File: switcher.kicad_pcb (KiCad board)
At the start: 2 copper layers, 137.5 x 100 mm, 67 parts, among them K1 RELAY, P1 CONN_01X02, P10 CONN_01X04, P11 CONN_01X04, P12 CONN_01X04, P13 CONN_01X04, P2 CONN_01X02, P3 CONN_01X04, P4 CONN_01X04, P5 CONN_01X04, P6 CONN_01X02, P7 CONN_01X04, P8 CONN_01X04, P9 BDM, Q1 BC237, SW1 RESET, SW2 SP3T, T1 TRANSFO, U1 MC9S08SH8, U10 4N25, U11 4N25, U12 4N25, U13 4N25, U14 4N25, U2 78L05, U3 4N25, U4 4N25, U5 4N25, U6 4N25, U7 4N25, U8 4N25, U9 4N25

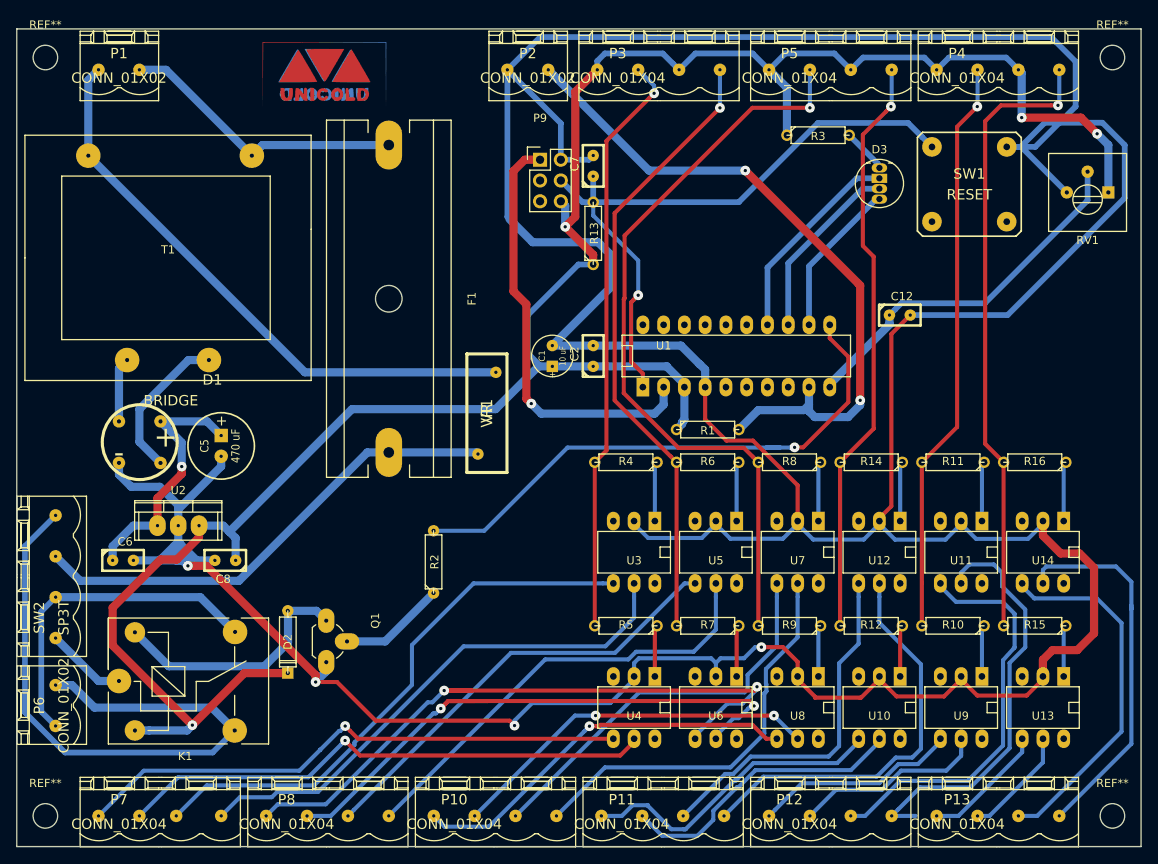
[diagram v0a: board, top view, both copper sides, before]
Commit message: cambio relay
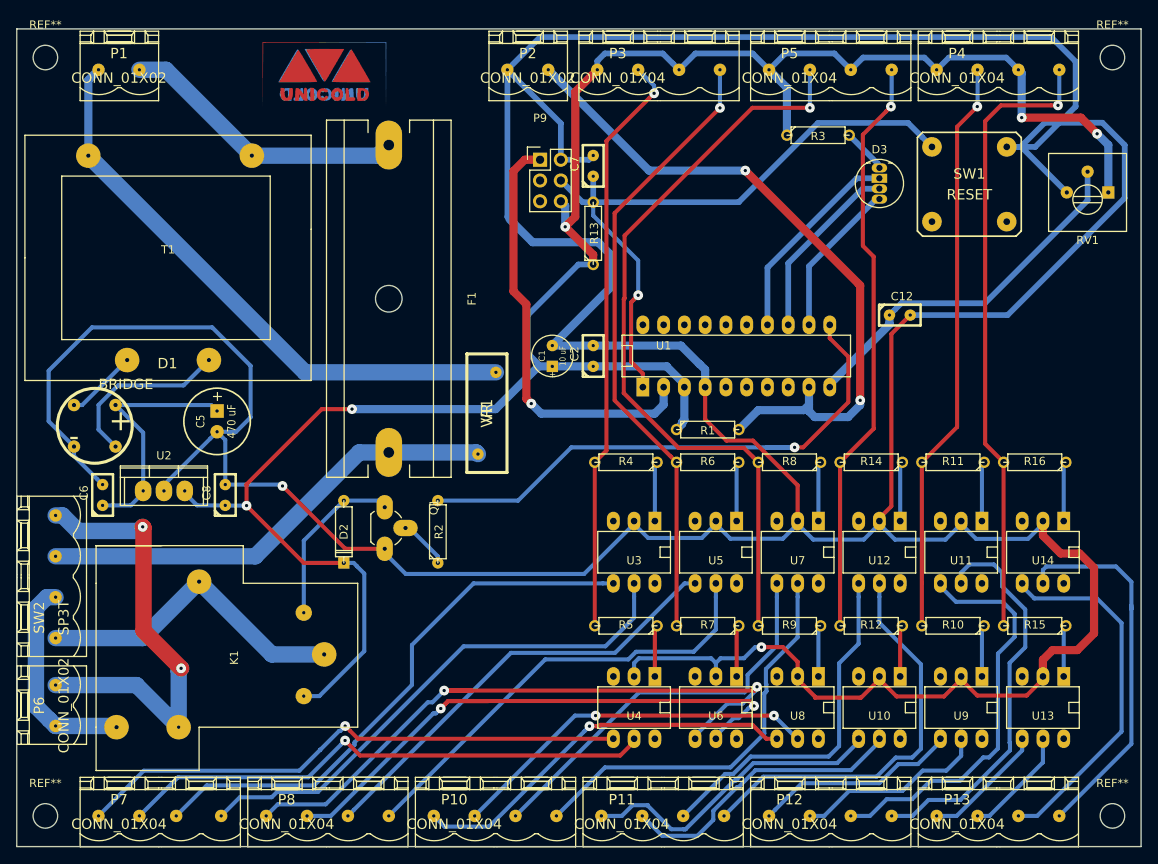
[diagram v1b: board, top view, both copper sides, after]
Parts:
- K1: footprint Relays_ThroughHole:Relay_SANYOU_SRD_Series_Form_C -> locales:RELAY-HJQ-15F
- moved Q1 15.6 mm to (119.5, 88.5)
- moved D2 15.1 mm to (114.5, 91.5)
- moved K1 13.5 mm to (100.2, 106.9), turned to 90 degrees
- moved C6 8.38 mm to (85.0, 87.0), turned to 90 degrees
- moved C8 8.00 mm to (100.0, 87.0), turned to 90 degrees
- moved D1 5.85 mm to (81.5, 76.0)
- moved U2 4.60 mm to (92.5, 86.5)
- moved R2 3.72 mm to (126.0, 91.5)
- moved C5 3.04 mm to (99.0, 78.0)
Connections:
- K1 pad 1: /C -> /NC
- K1 pad 2: /vreg -> /NA
- K1 pad 3: /NA -> /C
- K1 pad 4: /NC -> /vreg
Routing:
- net /C: track 9.92 -> 39.4 mm
- net /NA: track 78.6 -> 55.4 mm, vias 0 -> 2
- net /vreg: track 275.7 -> 255.9 mm, vias 4 -> 5
- net /NC: track 40.9 -> 25.9 mm
- net GND: track 557.2 -> 570.7 mm, vias 4 -> 2
- net Net-(D2-Pad1): track 30.7 -> 21.1 mm
- net Net-(Q1-Pad2): track 13.0 -> 6.20 mm
- net Net-(D1-Pad2): track 18.6 -> 21.7 mm
- net Net-(P12-Pad4): track 51.7 -> 49.0 mm
- net Net-(R2-Pad2): track 69.9 -> 71.3 mm
- net /24V: track 31.4 -> 30.5 mm, vias 1 -> 0
- net Net-(D1-Pad4): track 7.91 -> 8.78 mm
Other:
- net class Default: clearance 0.4 -> 0.35
- net class POTENCIA: trace_width 1 -> 2
- rule trace_clearance: 0.4 -> 0.35

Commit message: di vueltas el relay
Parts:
- K1: moved to B.Cu
- turned K1 to 270 degrees
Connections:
- K1 pad 4: /vreg -> Net-(D2-Pad1)
- K1 pad 5: Net-(D2-Pad1) -> /vreg
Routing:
- net /C: track 39.4 -> 54.7 mm
- net /NC: track 25.9 -> 33.8 mm
- net /vreg: track 255.9 -> 258.6 mm
- net Net-(D2-Pad1): track 21.1 -> 21.9 mm
- net /NA: track 55.4 -> 55.2 mm, vias 2 -> 3
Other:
- net class Default: trace_width 0.5 -> 2
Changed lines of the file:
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@@
     (links 125)
     (no_connects 0)
-    (area 74.449999 29.949999 212.050001 130.050001)
+    (area 71.361474 28.2245 217.140046 132.37626)
     (thickness 1.6)
     (drawings 4)
-    (tracks 668)
+    (tracks 681)
     (zones 0)
     (modules 67)
@@
   )
   (setup
-    (last_trace_width 0.5)
+    (last_trace_width 2)
     (trace_clearance 0.35)
     (zone_clearance 0.508)
@@
     (mod_text_size 1 1)
     (mod_text_width 0.15)
-    (pad_size 3 3)
-    (pad_drill 0.5)
+    (pad_size 2 2)
+    (pad_drill 0.4)
     (pad_to_mask_clearance 0)
     (aux_axis_origin 0 0)
@@
   (net_class Default "This is the default net class."
     (clearance 0.35)
-    (trace_width 0.5)
+    (trace_width 2)
     (via_dia 1.2)
     (via_drill 0.4)
@@
       (xy 5.87248 -0.74168) (xy 6.01472 -1.016) (xy 6.01472 -1.016)) (layer B.Cu) (width 0.00254))
   )
-  (module locales:RELAY-HJQ-15F (layer F.Cu)
-    (at 100.2 106.9 90)
-    (fp_text reference K1 (at 0 0.9 90) (layer F.SilkS)
-      (effects (font (size 1 1) (thickness 0.15)))
-    )
-    (fp_text value RELAY (at 0 -0.8 90) (layer F.Fab)
-      (effects (font (size 1 1) (thickness 0.15)))
-    )
-    (fp_line (start 9.1 2) (end 9.1 16) (layer F.SilkS) (width 0.15))
-    (fp_line (start 13.7 -16) (end 13.7 2) (layer F.SilkS) (width 0.15))
-    (fp_line (start 13.7 2) (end 9.1 2) (layer F.SilkS) (width 0.15))
-    (fp_line (start 13.7 -16) (end 9.1 -16) (layer F.SilkS) (width 0.15))
-    (fp_line (start 9.1 16) (end -8.5 16) (layer F.SilkS) (width 0.15))
-    (fp_line (start 13.7 -8) (end 13.7 -16) (layer F.SilkS) (width 0.15))
-    (fp_line (start -8.5 -3.4) (end -8.5 16) (layer F.SilkS) (width 0.15))
-    (fp_line (start -13.8 -3.4) (end -13.8 -16) (layer F.SilkS) (width 0.15))
-    (fp_line (start -13.8 -16) (end -8.5 -16) (layer F.SilkS) (width 0.15))
-    (fp_line (start -13.8 -3.4) (end -8.5 -3.4) (layer F.SilkS) (width 0.15))
-    (fp_line (start -8.5 -16) (end 9.1 -16) (layer F.SilkS) (width 0.15))
-    (pad 1 thru_hole circle (at -8.5 -13.5 90) (size 3 3) (drill 0.5) (layers *.Cu *.Mask F.SilkS)
+  (module locales:RELAY-HJQ-15F (layer B.Cu)
+    (at 100.2 106.9 270)
+    (fp_text reference K1 (at 0 -0.9 270) (layer B.SilkS)
+      (effects (font (size 1 1) (thickness 0.15)) (justify mirror))
+    )
+    (fp_text value RELAY (at 0 0.8 270) (layer B.Fab)
+      (effects (font (size 1 1) (thickness 0.15)) (justify mirror))
+    )
+    (fp_line (start 9.1 -2) (end 9.1 -16) (layer B.SilkS) (width 0.15))
+    (fp_line (start 13.7 16) (end 13.7 -2) (layer B.SilkS) (width 0.15))
+    (fp_line (start 13.7 -2) (end 9.1 -2) (layer B.SilkS) (width 0.15))
+    (fp_line (start 13.7 16) (end 9.1 16) (layer B.SilkS) (width 0.15))
+    (fp_line (start 9.1 -16) (end -8.5 -16) (layer B.SilkS) (width 0.15))
+    (fp_line (start 13.7 8) (end 13.7 16) (layer B.SilkS) (width 0.15))
+    (fp_line (start -8.5 3.4) (end -8.5 -16) (layer B.SilkS) (width 0.15))
+    (fp_line (start -13.8 3.4) (end -13.8 16) (layer B.SilkS) (width 0.15))
+    (fp_line (start -13.8 16) (end -8.5 16) (layer B.SilkS) (width 0.15))
+    (fp_line (start -13.8 3.4) (end -8.5 3.4) (layer B.SilkS) (width 0.15))
+    (fp_line (start -8.5 16) (end 9.1 16) (layer B.SilkS) (width 0.15))
+    (pad 1 thru_hole circle (at -8.5 13.5 270) (size 3 3) (drill 0.5) (layers *.Cu *.Mask B.SilkS)
       (net 10 /NC))
-    (pad 2 thru_hole circle (at -8.5 -5.9 90) (size 3 3) (drill 0.4) (layers *.Cu *.Mask F.SilkS)
+    (pad 2 thru_hole circle (at -8.5 5.9 270) (size 3 3) (drill 0.4) (layers *.Cu *.Mask B.SilkS)
       (net 8 /NA))
-    (pad 3 thru_hole circle (at 9.3 -3.4 90) (size 3 3) (drill 0.5) (layers *.Cu *.Mask F.SilkS)
+    (pad 3 thru_hole circle (at 9.3 3.4 270) (size 3 3) (drill 0.5) (layers *.Cu *.Mask B.SilkS)
       (net 9 /C))
-    (pad 4 thru_hole circle (at -4.7 9.4 90) (size 2 2) (drill 0.4) (layers *.Cu *.Mask F.SilkS)
-      (net 2 /vreg))
-    (pad 5 thru_hole circle (at 5.5 9.4 90) (size 2 2) (drill 0.4) (layers *.Cu *.Mask F.SilkS)
+    (pad 4 thru_hole circle (at -4.7 -9.4 270) (size 2 2) (drill 0.4) (layers *.Cu *.Mask B.SilkS)
       (net 1 "Net-(D2-Pad1)"))
-    (pad 6 thru_hole circle (at 0.4 11.9 90) (size 3 3) (drill 0.5) (layers *.Cu *.Mask F.SilkS)
+    (pad 5 thru_hole circle (at 5.5 -9.4 270) (size 2 2) (drill 0.4) (layers *.Cu *.Mask B.SilkS)
+      (net 2 /vreg))
+    (pad 6 thru_hole circle (at 0.4 -11.9 270) (size 3 3) (drill 0.5) (layers *.Cu *.Mask B.SilkS)
       (net 9 /C))
   )
@@
   (gr_line (start 74.5 130) (end 74.5 30) (angle 90) (layer Edge.Cuts) (width 0.1))
   (gr_line (start 74.5 130) (end 212 130) (angle 90) (layer Edge.Cuts) (width 0.1))
+  (segment (start 111.013284 100.786716) (end 111.013284 91.176716) (width 0.5) (layer B.Cu) (net 1))
+  (segment (start 111.013284 91.176716) (end 114.5 87.69) (width 0.5) (layer B.Cu) (net 1))
+  (segment (start 109.6 102.2) (end 111.013284 100.786716) (width 0.5) (layer B.Cu) (net 1))
   (segment (start 114.5 87.69) (end 118.69 87.69) (width 0.5) (layer B.Cu) (net 1))
   (segment (start 118.69 87.69) (end 119.5 88.5) (width 0.5) (layer B.Cu) (net 1))
-  (segment (start 109.6 101.4) (end 109.6 92.59) (width 0.5) (layer B.Cu) (net 1))
-  (segment (start 109.6 92.59) (end 114.5 87.69) (width 0.5) (layer B.Cu) (net 1))
-  (segment (start 109.6 111.6) (end 111.5 111.6) (width 0.5) (layer B.Cu) (net 2))
-  (segment (start 111.5 111.6) (end 117 106.1) (width 0.5) (layer B.Cu) (net 2))
+  (segment (start 109.6 112.4) (end 110.599999 111.400001) (width 0.5) (layer B.Cu) (net 2))
+  (segment (start 110.599999 111.400001) (end 112.769999 111.400001) (width 0.5) (layer B.Cu) (net 2))
+  (segment (start 112.769999 111.400001) (end 117.57 106.6) (width 0.5) (layer B.Cu) (net 2))
+  (segment (start 117.57 97.1815) (end 116.1 95.7115) (width 0.5) (layer B.Cu) (net 2))
+  (segment (start 117.57 106.6) (end 117.57 97.1815) (width 0.5) (layer B.Cu) (net 2))
   (segment (start 114.5 95.31) (end 115.71 95.31) (width 0.5) (layer B.Cu) (net 2))
   (segment (start 116.1 95.7) (end 116.1 95.7115) (width 0.5) (layer B.Cu) (net 2))
   (segment (start 115.71 95.31) (end 116.1 95.7) (width 0.5) (layer B.Cu) (net 2))
   (segment (start 117 96.6115) (end 116.1 95.7115) (width 0.5) (layer B.Cu) (net 2))
-  (segment (start 117 106.1) (end 117 96.6115) (width 0.5) (layer B.Cu) (net 2))
   (segment (start 102.6 85.7) (end 111.8 76.5) (width 0.5) (layer F.Cu) (net 2))
   (segment (start 111.8 76.5) (end 115.5 76.5) (width 0.5) (layer F.Cu) (net 2))
@@
   (segment (start 103.25 45.5) (end 118.704 45.5) (width 2) (layer B.Cu) (net 7))
   (segment (start 118.704 45.5) (end 120 44.204) (width 2) (layer B.Cu) (net 7))
+  (segment (start 89.98 100.85) (end 89.98 103.58) (width 2) (layer F.Cu) (net 8))
+  (segment (start 89.98 103.58) (end 90 103.6) (width 2) (layer F.Cu) (net 8))
+  (segment (start 94.3 98.4) (end 92.43 98.4) (width 2) (layer B.Cu) (net 8))
+  (segment (start 92.43 98.4) (end 89.98 100.85) (width 2) (layer B.Cu) (net 8))
+  (via (at 89.98 100.85) (size 1.2) (drill 0.4) (layers F.Cu B.Cu) (net 8))
+  (segment (start 79.25 110.25) (end 92.55 110.25) (width 2) (layer B.Cu) (net 8))
+  (segment (start 92.55 110.25) (end 94.6 108.2) (width 2) (layer B.Cu) (net 8))
   (segment (start 79.25 89.5) (end 80.1 89.5) (width 2) (layer B.Cu) (net 8))
-  (segment (start 94.3 108.5) (end 94.3 115.4) (width 2) (layer B.Cu) (net 8))
-  (segment (start 94.6 108.2) (end 94.3 108.5) (width 2) (layer B.Cu) (net 8))
   (via (at 94.6 108.2) (size 1.2) (drill 0.4) (layers F.Cu B.Cu) (net 8))
   (segment (start 90 103.6) (end 94.6 108.2) (width 2) (layer F.Cu) (net 8))
@@
   (segment (start 82 91.4) (end 89.4 91.4) (width 2) (layer B.Cu) (net 8))
   (segment (start 80.1 89.5) (end 82 91.4) (width 2) (layer B.Cu) (net 8))
-  (segment (start 79.25 110.25) (end 89.15 110.25) (width 2) (layer B.Cu) (net 8))
-  (segment (start 89.15 110.25) (end 94.3 115.4) (width 2) (layer B.Cu) (net 8))
+  (segment (start 96.8 116.2) (end 96.8 114.07868) (width 2) (layer B.Cu) (net 9))
+  (segment (start 96.8 114.07868) (end 103.57868 107.3) (width 2) (layer B.Cu) (net 9))
+  (segment (start 103.57868 107.3) (end 109.97868 107.3) (width 2) (layer B.Cu) (net 9))
+  (segment (start 109.97868 107.3) (end 112.1 107.3) (width 2) (layer B.Cu) (net 9))
+  (segment (start 105.7 106.5) (end 102.80291 103.60291) (width 2) (layer B.Cu) (net 9))
+  (segment (start 96.29709 103.60291) (end 102.80291 103.60291) (width 2) (layer B.Cu) (net 9))
+  (segment (start 95.4 104.5) (end 96.29709 103.60291) (width 2) (layer B.Cu) (net 9))
+  (segment (start 79.25 104.5) (end 95.4 104.5) (width 2) (layer B.Cu) (net 9))
   (segment (start 112.1 106.5) (end 105.7 106.5) (width 2) (layer B.Cu) (net 9))
-  (segment (start 105.7 106.5) (end 96.8 97.6) (width 2) (layer B.Cu) (net 9))
-  (segment (start 79.25 104.5) (end 89.9 104.5) (width 2) (layer B.Cu) (net 9))
-  (segment (start 89.9 104.5) (end 96.8 97.6) (width 2) (layer B.Cu) (net 9))
+  (segment (start 79.25 99.5) (end 85.6 99.5) (width 2) (layer B.Cu) (net 10))
+  (segment (start 85.6 99.5) (end 86.7 98.4) (width 2) (layer B.Cu) (net 10))
   (segment (start 79.25 99.5) (end 78.17237 99.5) (width 2) (layer B.Cu) (net 10))
   (segment (start 78.17237 99.5) (end 76.84999 100.82238) (width 2) (layer B.Cu) (net 10))
